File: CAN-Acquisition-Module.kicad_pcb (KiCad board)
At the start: 4 copper layers, 95 x 65 mm, 219 parts, among them J1 Conn_01x04, J10 OSTVN04A150, J11 OSTVN04A150, J12 OSTVN04A150, J13 OSTVN04A150, J2 Conn_01x02, J3 Conn_01x03, J4 Conn_02x05_Odd_Even, J5 OSTVN04A150, J6 OSTVN04A150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

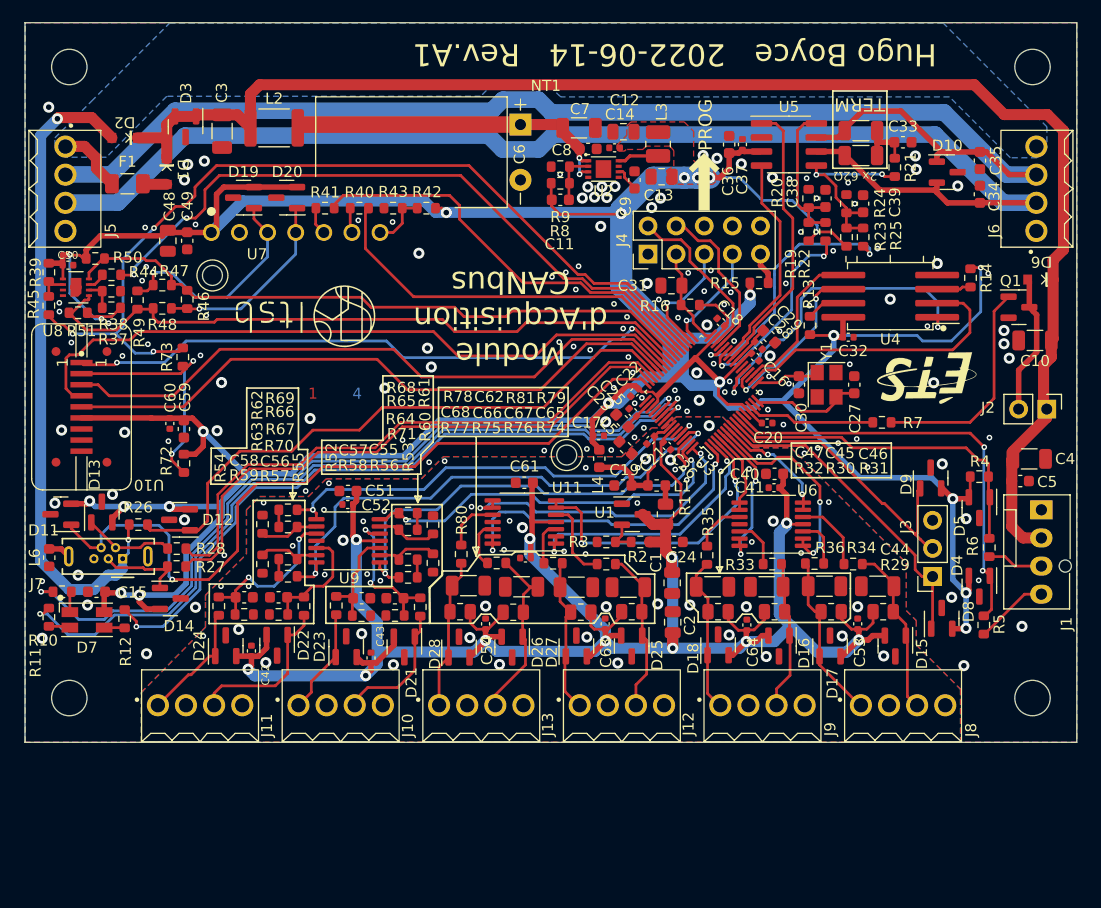
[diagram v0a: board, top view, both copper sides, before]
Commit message: Rev. A2
U1 had wrong pinout. NT1 label removed from silk. Green LED resistor increased in value
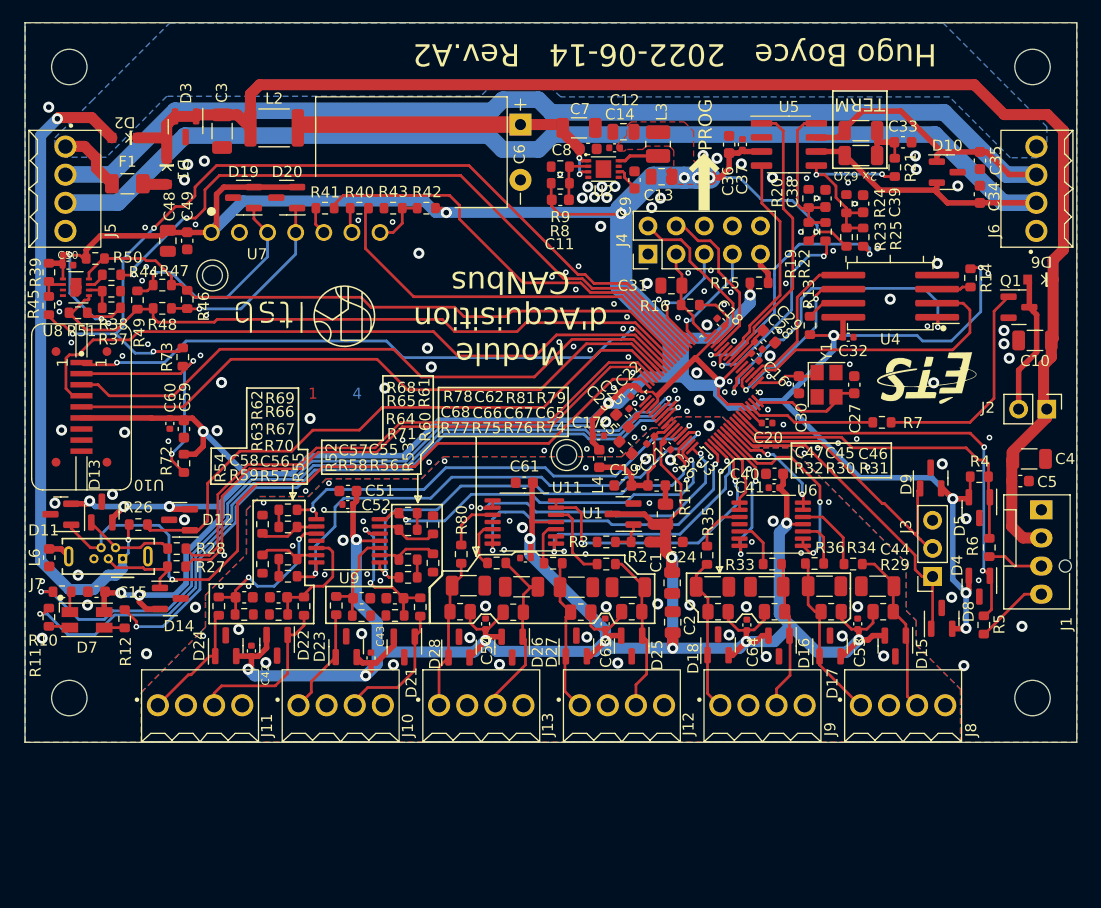
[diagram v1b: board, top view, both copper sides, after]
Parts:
- F1: value PPTC, 50-500mA, 60V -> 100 mA
- R11: value 120 Ω -> 220 Ω
- moved U1 0.83 mm to (74.0, 69.4), turned to 180 degrees
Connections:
- U1 pad 1: GNDA -> Net-(R2-Pad2)
- U1 pad 2: Net-(R2-Pad2) -> GNDA
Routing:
- net Net-(C7-Pad1): track 6.23 -> 27.3 mm
- net Net-(C6-Pad1): track 21.1 -> 0.00 mm
- net +1V8: track 197.7 -> 200.5 mm
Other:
- board text added: "Hugo Boyce 2022-06-14 Rev.A2"
- board text removed: "Hugo Boyce 2022-06-14 Rev.A1"

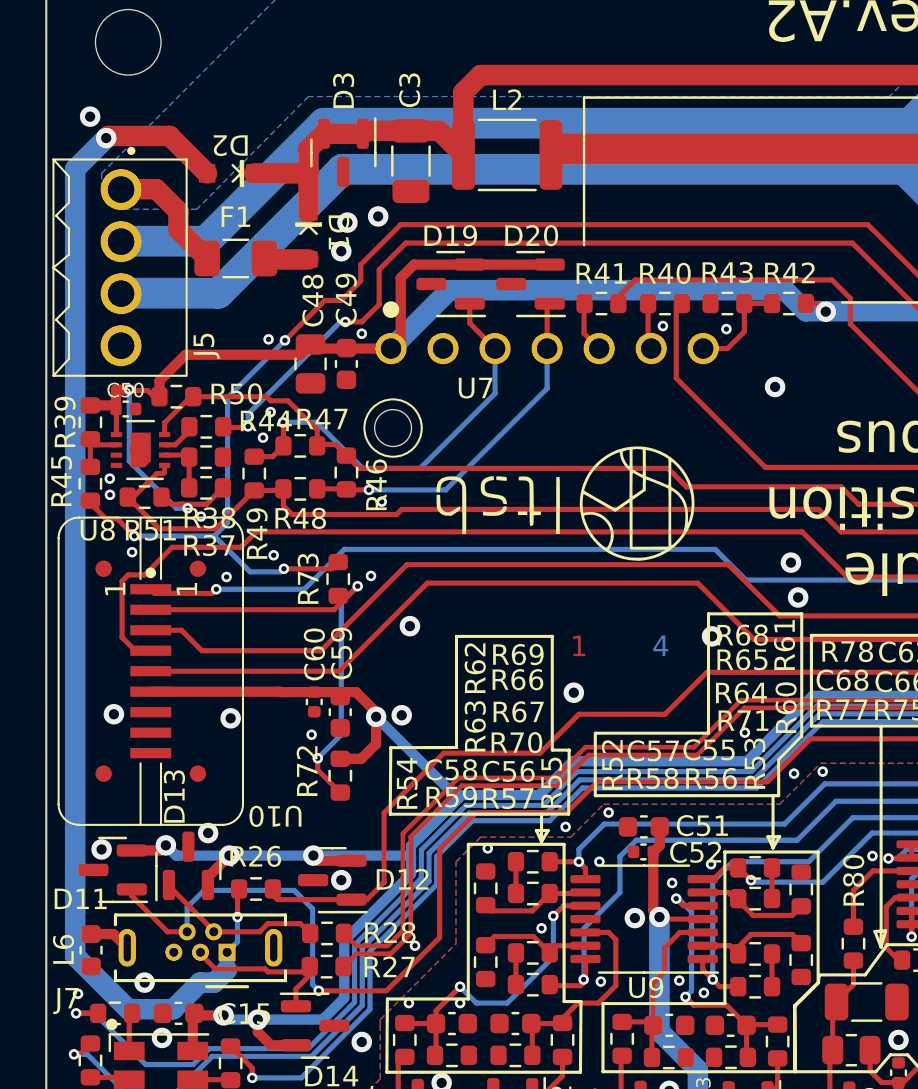
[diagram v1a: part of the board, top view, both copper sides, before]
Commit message: Changed the node where the V_USB diode connects.
Having the V_USB go through the VBUS inductor caused the voltage to sag too low.
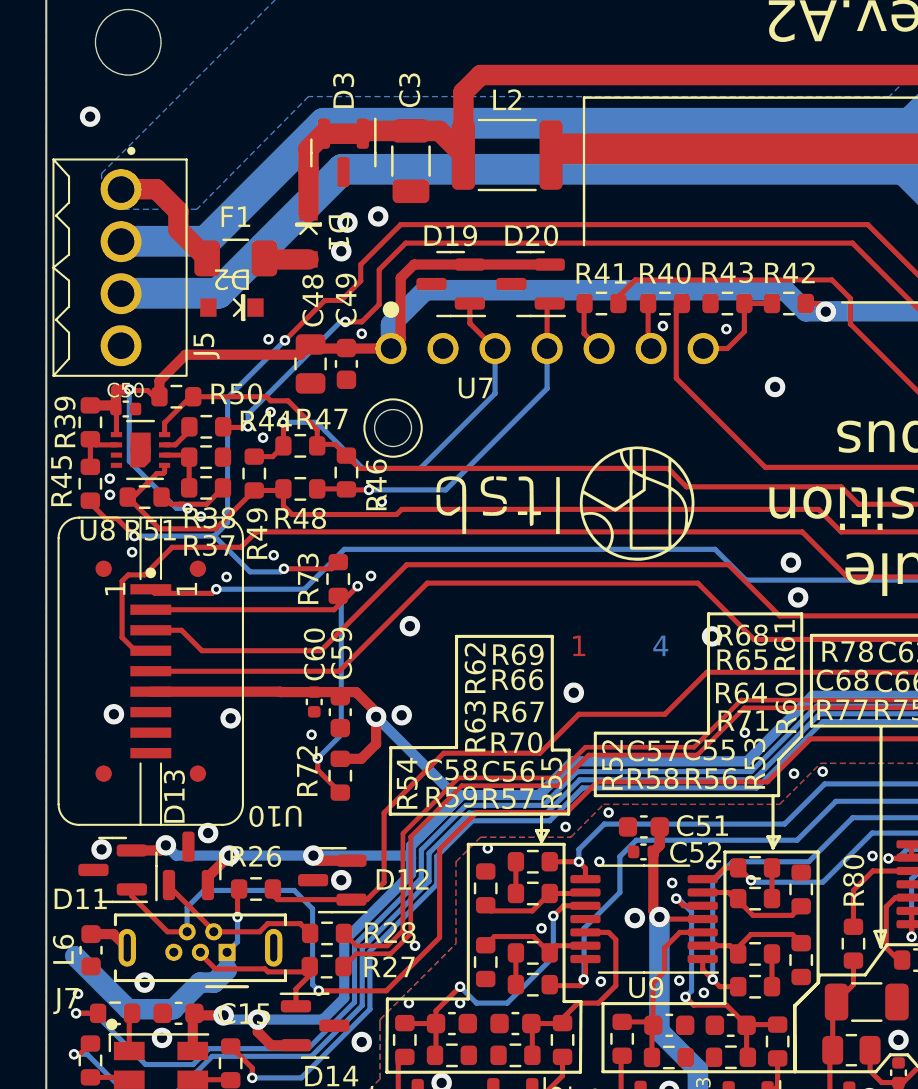
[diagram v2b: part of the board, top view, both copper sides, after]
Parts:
- moved D2 6.55 mm to (29.1, 42.0)
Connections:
- D2 pad 1: VBUS -> Net-(C6-Pad1)
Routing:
- net /Power/V_USB: track 59.8 -> 13.5 mm, vias 2 -> 1
- net VBUS: track 133.8 -> 131.1 mm
- net +3V3: track 380.7 -> 381.4 mm
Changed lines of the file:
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@@
   )
   (footprint "CAN-Acquisition-Module:Toshiba_USC" (layer "F.Cu")
-    (at 29 35.4 180)
+    (at 29.06 41.95 180)
     (property "Mfr." "Toshiba")
     (property "P/N" "CUS05S40,H3F")
@@
     (fp_rect (start -1.25 -0.625) (end 1.25 0.625) (layer "F.Fab") (width 0.1) (fill none))
     (pad "1" smd rect (at -1.15 0 180) (size 0.8 0.9) (layers "F.Cu" "F.Paste" "F.Mask")
-      (net 3 "VBUS") (pinfunction "K") (pintype "passive"))
+      (net 5 "Net-(C6-Pad1)") (pinfunction "K") (pintype "passive"))
     (pad "2" smd rect (at 1.15 0 180) (size 0.8 0.9) (layers "F.Cu" "F.Paste" "F.Mask")
       (net 15 "/Power/V_USB") (pinfunction "A") (pintype "passive"))
@@
   (via (at 90.1 72.9) (size 0.514) (drill 0.254) (layers "F.Cu" "B.Cu") (free) (net 2))
   (segment (start 113.8 34.75) (end 113.8 45.5) (width 1) (layer "F.Cu") (net 3))
-  (segment (start 30.15 35.4) (end 32.65 35.4) (width 1) (layer "F.Cu") (net 3))
   (segment (start 109.125 64.5) (end 109.225 64.4) (width 1) (layer "F.Cu") (net 3))
   (segment (start 112.35 33.3) (end 113.8 34.75) (width 1) (layer "F.Cu") (net 3))
@@
   (segment (start 112.7 55.206582) (end 112.7 53.7) (width 1) (layer "F.Cu") (net 3))
   (segment (start 32.8 37.3) (end 32.8 35.25) (width 1) (layer "F.Cu") (net 3))
-  (segment (start 32.65 35.4) (end 32.8 35.25) (width 1) (layer "F.Cu") (net 3))
   (segment (start 109.125 66.4) (end 109.125 70.525) (width 1) (layer "F.Cu") (net 3))
   (segment (start 40.3625 31.4375) (end 41.2 30.6) (width 1) (layer "F.Cu") (net 3))
@@
   (segment (start 34.54544 75.65456) (end 34.54544 72.85456) (width 0.5) (layer "B.Cu") (net 7))
   (segment (start 28.86025 76.70525) (end 33.49475 76.70525) (width 0.5) (layer "B.Cu") (net 7))
-  (segment (start 39.677701 41.1) (end 36.827701 43.95) (width 1) (layer "B.Cu") (net 7))
   (segment (start 93.05 53.25) (end 93.05 54.55) (width 0.5) (layer "B.Cu") (net 7))
   (segment (start 85.5 49.6) (end 85.5 50.35) (width 1) (layer "B.Cu") (net 7))
@@
   (segment (start 37.80544 68.220346) (end 38.212893 67.812893) (width 0.5) (layer "B.Cu") (net 7))
   (segment (start 40.099643 65.926143) (end 36.1 61.9265) (width 0.5) (layer "B.Cu") (net 7))
+  (segment (start 57.08 42.13) (end 56.05 41.1) (width 1) (layer "B.Cu") (net 7))
   (segment (start 100.575 53.25) (end 101.075 53.75) (width 0.25) (layer "B.Cu") (net 7))
   (segment (start 106.325 51.1) (end 106.325 47.125) (width 0.25) (layer "B.Cu") (net 7))
@@
   (segment (start 37.80544 68.80544) (end 37.80544 68.220346) (width 0.5) (layer "B.Cu") (net 7))
   (segment (start 89.3 41.05) (end 91.55 43.3) (width 0.25) (layer "B.Cu") (net 7))
-  (segment (start 73.73 42.13) (end 57.08 42.13) (width 1) (layer "B.Cu") (net 7))
   (segment (start 82.4 57.8) (end 82.451501 57.748499) (width 0.5) (layer "B.Cu") (net 7))
   (segment (start 101.9 66.1) (end 99.4 66.1) (width 0.5) (layer "B.Cu") (net 7))
   (segment (start 101.075 53.75) (end 103.675 53.75) (width 0.25) (layer "B.Cu") (net 7))
   (segment (start 34.54544 72.85456) (end 37.80544 69.59456) (width 0.5) (layer "B.Cu") (net 7))
-  (segment (start 57.08 42.13) (end 56.05 41.1) (width 1) (layer "B.Cu") (net 7))
   (segment (start 80.75 39) (end 81.85 39) (width 2) (layer "B.Cu") (net 7))
   (segment (start 86.6 41.05) (end 88.75 41.05) (width 0.25) (layer "B.Cu") (net 7))
+  (segment (start 36.827701 42.772299) (end 36.827701 43.95) (width 1) (layer "B.Cu") (net 7))
   (segment (start 91.55 43.8) (end 91.45 43.9) (width 0.25) (layer "B.Cu") (net 7))
   (segment (start 88.75 41.05) (end 89.05 41.05) (width 0.25) (layer "B.Cu") (net 7))
@@
   (segment (start 45.70152 64.09848) (end 54.20152 64.09848) (width 0.5) (layer "B.Cu") (net 7))
   (segment (start 72.72 59.36) (end 73.64 59.36) (width 1) (layer "B.Cu") (net 7))
+  (segment (start 38.5 41.1) (end 36.827701 42.772299) (width 1) (layer "B.Cu") (net 7))
   (segment (start 38.212893 67.812893) (end 40.280346 65.74544) (width 0.5) (layer "B.Cu") (net 7))
   (segment (start 88.45 59.15) (end 86.525 59.15) (width 0.5) (layer "B.Cu") (net 7))
-  (segment (start 56.05 41.1) (end 39.677701 41.1) (width 1) (layer "B.Cu") (net 7))
   (segment (start 71.18 60.9) (end 72.72 59.36) (width 0.5) (layer "B.Cu") (net 7))
   (segment (start 54.20152 64.09848) (end 57.4 60.9) (width 0.5) (layer "B.Cu") (net 7))
   (segment (start 28.655 76.5) (end 28.86025 76.70525) (width 0.5) (layer "B.Cu") (net 7))
   (segment (start 37.80544 69.59456) (end 37.80544 68.80544) (width 0.5) (layer "B.Cu") (net 7))
+  (segment (start 73.73 42.13) (end 57.08 42.13) (width 1) (layer "B.Cu") (net 7))
   (segment (start 76 57) (end 79.462896 57) (width 1) (layer "B.Cu") (net 7))
   (segment (start 79.462896 57) (end 80.211395 57.748499) (width 1) (layer "B.Cu") (net 7))
+  (segment (start 56.05 41.1) (end 38.5 41.1) (width 1) (layer "B.Cu") (net 7))
   (segment (start 85.875 59.8) (end 83.6 59.8) (width 0.5) (layer "B.Cu") (net 7))
   (segment (start 80.211395 57.748499) (end 82.451501 57.748499) (width 1) (layer "B.Cu") (net 7))
@@
   (segment (start 82.451501 57.748499) (end 82.747792 57.452208) (width 1) (layer "B.Cu") (net 7))
   (segment (start 103.8 68) (end 103.8 75.3) (width 0.5) (layer "B.Cu") (net 7))
+  (segment (start 73.85 42.25) (end 73.73 42.13) (width 1) (layer "B.Cu") (net 7))
   (segment (start 78.575 53.525) (end 78.575 56.4) (width 2) (layer "B.Cu") (net 7))
   (segment (start 37.80544 68.80544) (end 37.7 68.7) (width 0.5) (layer "B.Cu") (net 7))
-  (segment (start 73.85 42.25) (end 73.73 42.13) (width 1) (layer "B.Cu") (net 7))
   (segment (start 26.3375 68.7) (end 25.8375 68.2) (width 0.5) (layer "B.Cu") (net 7))
   (segment (start 105 76.5) (end 105 79.7) (width 0.5) (layer "B.Cu") (net 7))
@@
   (segment (start 30.65 39.55) (end 30.7 39.6) (width 1) (layer "F.Cu") (net 14))
   (segment (start 30.7 39.6) (end 32.8 39.6) (width 1) (layer "F.Cu") (net 14))
-  (segment (start 22.925 33.675) (end 23.03 33.57) (width 1) (layer "F.Cu") (net 15))
-  (segment (start 23.03 33.57) (end 26.02 33.57) (width 1) (layer "F.Cu") (net 15))
-  (segment (start 26.02 33.57) (end 27.85 35.4) (width 1) (layer "F.Cu") (net 15))
   (segment (start 29.335 70.4075) (end 29.4125 70.33) (width 0.25) (layer "F.Cu") (net 15))
   (segment (start 29.335 71.7) (end 29.335 70.4075) (width 0.25) (layer "F.Cu") (net 15))
   (via (at 29.335 71.7) (size 0.514) (drill 0.254) (layers "F.Cu" "B.Cu") (net 15))
-  (via (at 22.925 33.675) (size 1) (drill 0.5) (layers "F.Cu" "B.Cu") (net 15))
   (segment (start 28.2 74.9) (end 28.825 74.275) (width 1) (layer "B.Cu") (net 15))
   (segment (start 29.335 72.91) (end 28.825 73.42) (width 0.25) (layer "B.Cu") (net 15))
-  (segment (start 21.410989 35.189011) (end 21.410989 73.610989) (width 1) (layer "B.Cu") (net 15))
   (segment (start 24 76.2) (end 26.2 76.2) (width 1) (layer "B.Cu") (net 15))
   (segment (start 27.5 74.9) (end 28.2 74.9) (width 1) (layer "B.Cu") (net 15))
   (segment (start 21.410989 73.610989) (end 24 76.2) (width 1) (layer "B.Cu") (net 15))
-  (segment (start 22.925 33.675) (end 21.410989 35.189011) (width 1) (layer "B.Cu") (net 15))
   (segment (start 26.2 76.2) (end 27.5 74.9) (width 1) (layer "B.Cu") (net 15))
   (segment (start 29.335 71.7) (end 29.335 72.91) (width 0.25) (layer "B.Cu") (net 15))

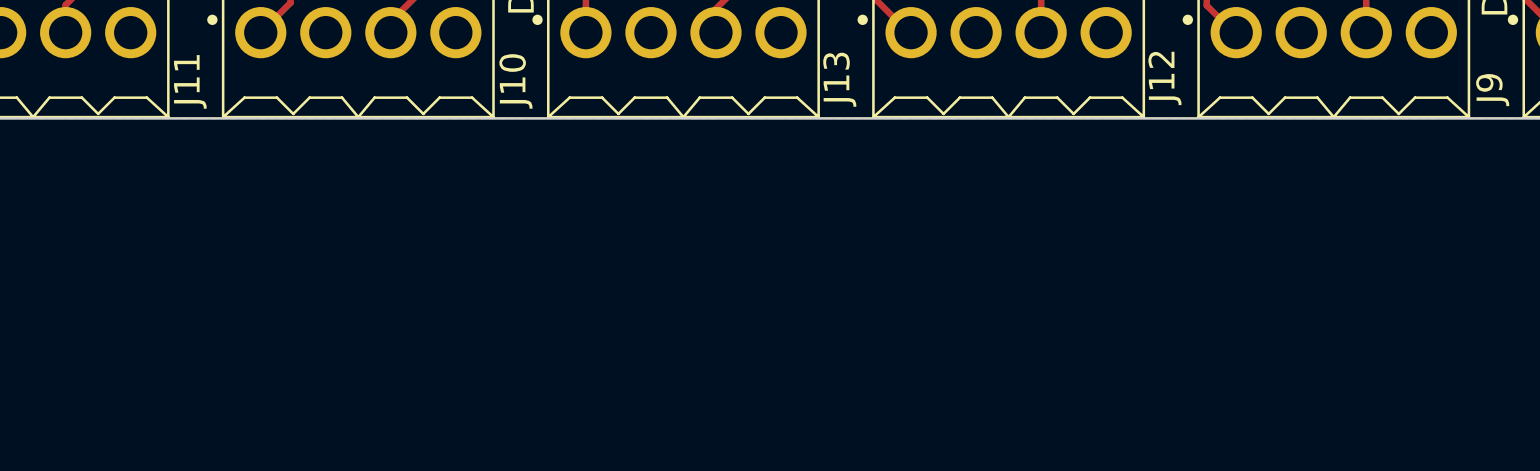
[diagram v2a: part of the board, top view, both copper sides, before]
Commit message: Added TODO
Route V_USB to C6, reduce screw terminal hole size, thermally isolate SHT3x sensor
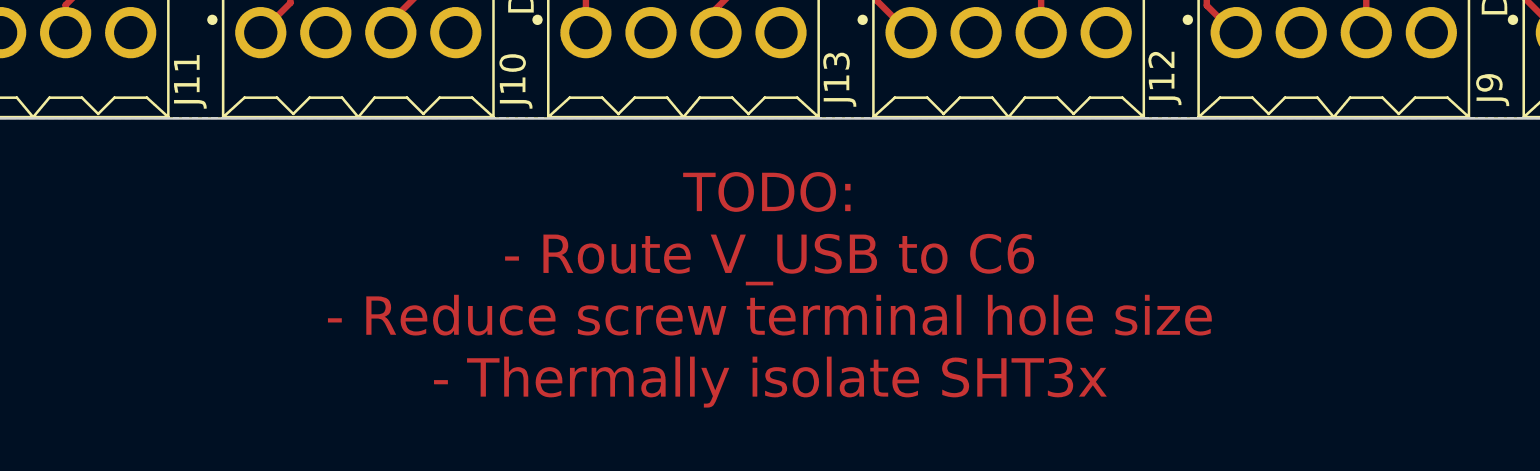
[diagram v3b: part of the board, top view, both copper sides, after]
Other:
- board text added: "TODO: - Route V_USB to C6 - Reduce screw terminal hole size - Thermally isolate SHT3x"
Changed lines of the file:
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@@
     (effects (font (size 1 1) (thickness 0.2)))
+  )
+  (gr_text "TODO:\n- Route V_USB to C6\n- Reduce screw terminal hole size\n- Thermally isolate SHT3x " (at 64.59 96.55) (layer "F.Cu")
+    (effects (font (size 1.5 1.5) (thickness 0.3)))
   )
   (gr_text "2" (at 47.25 58.5) (layer "In1.Cu")

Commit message: Rev.A2 pretty much finished
V USB bypasses inductor L2
Srew terminal pin holes size reduced
Thermally isolated SHT3x
Fixed U1 footprint
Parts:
- removed R46, R49, R73: Ω, Resistor_SMD:R_0603_1608Metric
- removed R47, R48: 0 Ω, Resistor_SMD:R_0603_1608Metric
- moved D2 15.7 mm to (43.7, 36.4), turned to 0 degrees
- moved R51 9.69 mm to (34.5, 51.8), turned to -90 degrees
- moved R39 9.28 mm to (30.7, 51.2), turned to 180 degrees
- moved R45 7.79 mm to (29.8, 49.0), turned to 90 degrees
- moved R50 7.68 mm to (33.0, 50.2), turned to 90 degrees
- moved R38 5.80 mm to (30.7, 54.3)
- moved C59 5.71 mm to (28.6, 61.7)
- moved C60 5.71 mm to (27.4, 61.2)
- moved R44 3.81 mm to (31.4, 49.0), turned to 90 degrees
- moved C50 3.62 mm to (21.2, 49.3), turned to -90 degrees
- moved R72 3.61 mm to (31.4, 62.7), turned to 90 degrees
- moved R37 3.51 mm to (30.7, 52.8)
- moved R40 2.93 mm to (53.0, 41.0), turned to -90 degrees
- moved D20 2.40 mm to (46.0, 40.8)
- moved D19 2.36 mm to (42.1, 40.8)
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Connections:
- D19 pad 1: Net-(D19-Pad1) -> /MCU/I2C_SCL
- D20 pad 1: Net-(D20-Pad1) -> /MCU/I2C_SDA
- U7 pad 3: Net-(D19-Pad1) -> /MCU/I2C_SCL
- U7 pad 4: Net-(D20-Pad1) -> /MCU/I2C_SDA
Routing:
- net /Power/V_USB: track 13.5 -> 102.1 mm, vias 1 -> 2
- net Net-(D19-Pad1): track 20.5 -> 0.00 mm, vias 1 -> 0
- net Net-(D20-Pad1): track 17.5 -> 0.00 mm, vias 1 -> 0
- net /MCU/PERIPHERAL_RESET: track 82.3 -> 64.9 mm, vias 3 -> 2
- net /MCU/I2C_SCL: track 58.3 -> 71.5 mm, vias 0 -> 1
- net /MCU/I2C_SDA: track 61.6 -> 73.9 mm, vias 0 -> 1
- net Net-(R72-Pad2): track 21.9 -> 10.6 mm
- net GND: track 0.45 -> 9.04 mm, vias 134 -> 135
- net Net-(R39-Pad2): track 2.74 -> 10.2 mm, vias 0 -> 2
- net Net-(R37-Pad2): track 2.74 -> 8.90 mm
- net Net-(R44-Pad1): track 1.65 -> 6.89 mm
- net Net-(C7-Pad1): track 27.3 -> 32.0 mm
- net /MCU/SCREEN_CLK: track 62.2 -> 58.7 mm, vias 0 -> 2
- net Net-(R40-Pad1): track 2.28 -> 5.38 mm
- net Net-(R42-Pad2): track 5.07 -> 7.59 mm
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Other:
- outline, holes or cut-outs redrawn
- board text added: "TODO: - VUSB bypass inductor L2 - Reduce screw terminal hole size - Thermally isolate SHT3x - U1 footprint fix"
- board text removed: "TODO: - Route V_USB to C6 - Reduce screw terminal hole size - Thermally isolate SHT3x"
